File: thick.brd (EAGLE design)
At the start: 37 x 25 mm, 27 parts, among them J1 43045-0400, Q1 SI2319DDS-T1-GE3, U1 ATTINY85-20SU

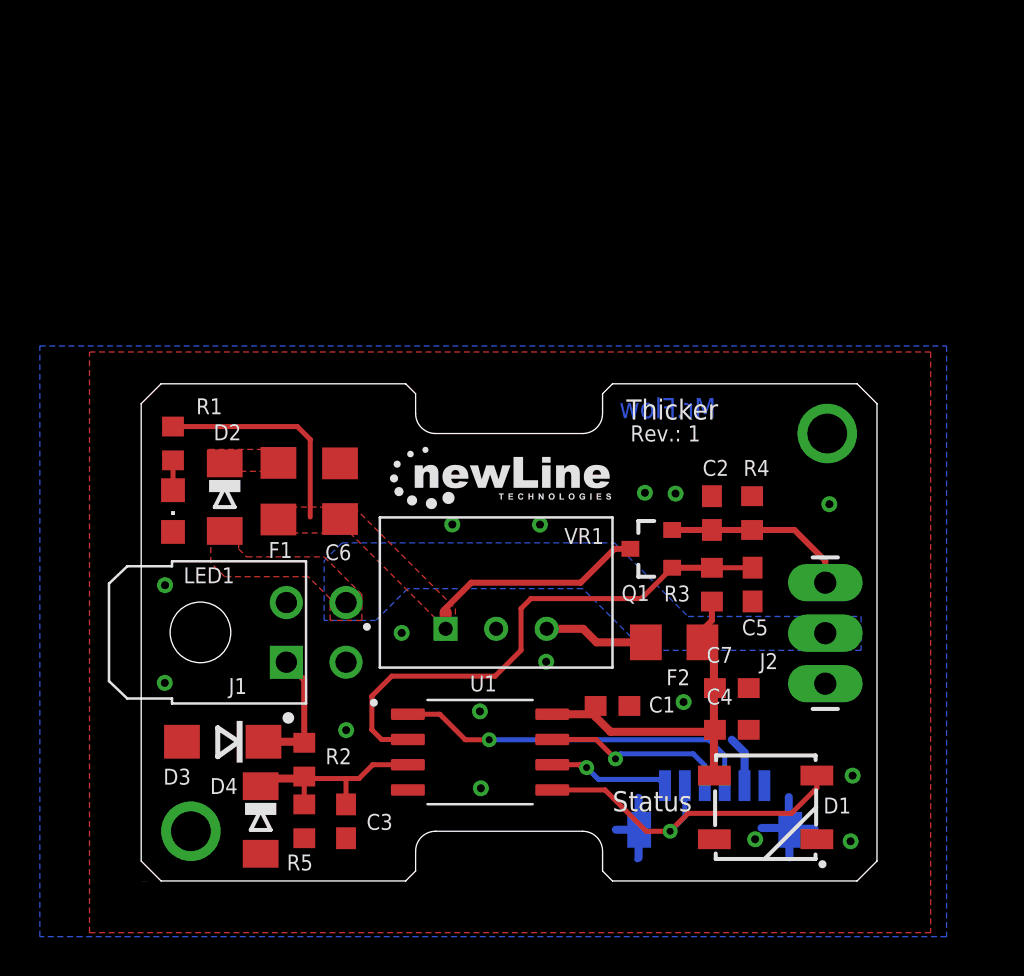
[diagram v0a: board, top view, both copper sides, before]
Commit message: Fixing
- sizes
- FPC connector
- Molex connector
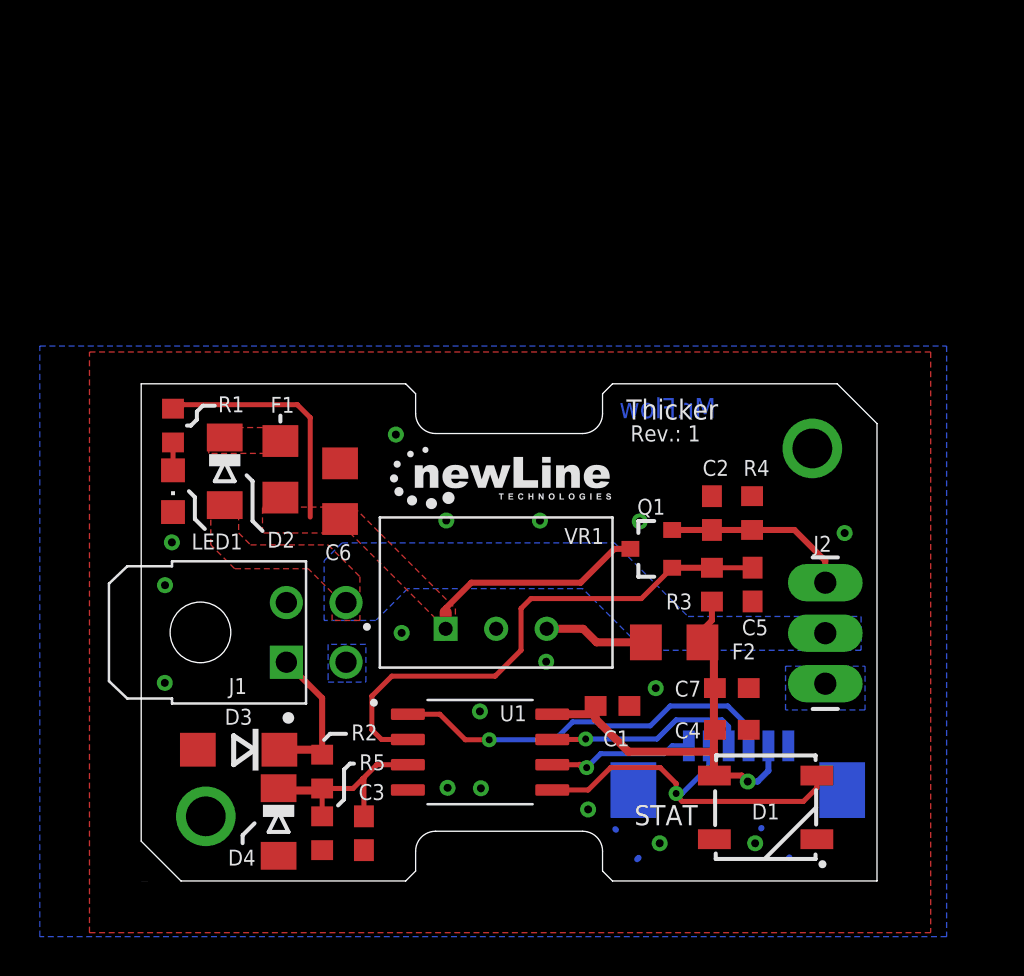
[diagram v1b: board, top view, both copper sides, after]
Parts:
- J4: value (none) -> F1003WR-S-06PT; device SparkFun-Connectors:1X06-1MM -> FloManEagle:1X06-1MM
- moved J4 2.33 mm to (30.0, 5.52)
- moved D2 1.30 mm to (4.20, 20.6)
- moved F1 1.10 mm to (7.00, 20.7)
- moved R5 1.08 mm to (9.10, 2.40)
- moved R2 1.08 mm to (9.10, 5.50)
- moved C3 1.08 mm to (11.2, 2.40)
- moved LED1 1.00 mm to (1.60, 19.6)
- moved D4 0.91 mm to (6.91, 2.96)
- moved R1 0.90 mm to (1.60, 22.9)
- moved D3 0.89 mm to (4.90, 6.60)
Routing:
- net GND: track 9.92 -> 0.22 mm, vias 18 -> 19
- net 5V: track 21.4 -> 23.6 mm, vias 0 -> 1
- net !RESET: track 18.3 -> 19.9 mm
- net MISO: track 6.11 -> 7.39 mm
- net VDD: track 22.8 -> 24.0 mm
- net SIGNAL: track 6.49 -> 7.65 mm
- net SCK: track 9.44 -> 10.4 mm
- net MOSI: track 18.3 -> 19.0 mm
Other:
- outline, holes or cut-outs redrawn
- board text added: "2021.06.30."
- board text added: "ISP"
- board text added: "STAT"
- board text removed: "2021.04.27."
- board text removed: "Programmer"
- board text removed: "Status"

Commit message: Javított végleges
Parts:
- added T1: (no value), transistor:SC59-BEC
- moved C5 5.16 mm to (25.6, 15.3)
- moved R3 5.06 mm to (25.6, 18.9)
- moved Q1 4.02 mm to (29.0, 19.0), turned to 270 degrees
- moved R4 3.73 mm to (34.4, 18.0)
- moved C2 3.54 mm to (32.2, 18.0)
- moved F2 0.36 mm to (27.1, 11.8)
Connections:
- removed net !IGN_EN: C5.1, Q1.1, R3.1, U1.2
- new net IGN_EN: C5.1, T1.B, U1.2
- new net N$1: Q1.1, R3.1, T1.C
- net 5V: no longer R3.2
- net GND: now also T1.E
- net IGNITION: now also Q1.3; no longer Q1.2
- net VDD: now also Q1.2, R3.2; no longer Q1.3
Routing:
- net !IGN_EN: track 26.8 -> 0.00 mm
- net IGN_EN: track 0.00 -> 23.1 mm
- net N$1: track 0.00 -> 8.14 mm
- net VDD: track 24.0 -> 28.2 mm
- net IGNITION: track 9.44 -> 7.77 mm
- net 5V: track 23.6 -> 22.0 mm
- net GND: vias 19 -> 18

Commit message: rev 2
new pcb design with gerbers
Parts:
- removed F2: (no value), adafruit:R1206
- removed VR1: VR05S05, TSR_1-24150:CONV_TSR_1-24150
- added C10, C8: 4.7uF, resistor:C1206
- added C11, C12: 0.1uF, resistor:C0603
- added C9: 100uF, resistor:E3,5-8
- added D5, D6: 0.5A/40V/420mV, SparkFun-DiscreteSemi:SOD-323
- added L1: TCK-047, TCK-047:TCK047
- added LED2: (no value), adafruit:CHIPLED_0805
- added R6: 10K, resistor:R0603
- added S1, S2: (no value), SparkFun-Switches:TACTILE_SWITCH_SMD_4.6X2.8MM
- added U$3: (no value), SparkFun-Aesthetics:ROHS_LOGO_0.18_IN
- added U$5: (no value), FloManEagle:MRFLOW_7_5MM
- added U2: TSR_0.5-2450, TSR_0.5-2450:TSR-0.5-2433
- C6: value 10uF -> 4.7uF
- C7: value 22uF -> 4.7uF; device resistor:C0603 -> resistor:C1206
- D3: value TVS -> tvs; device diode:DO214AC -> SparkFun-DiscreteSemi:SOD-323
- J1: value 43045-0400 -> (none); device 43045-0400:MOLEX_43045-0400 -> SparkFun-Connectors:1X03_LONGPADS
- moved J1 32.5 mm to (36.4, 18.5)
- moved U$1 32.3 mm to (25.0, 30.3)
- moved D3 31.4 mm to (32.2, 22.2), turned to 90 degrees
- moved J4 30.1 mm to (5.32, 22.8), flipped to the top, turned to 270 degrees
- moved D2 27.8 mm to (31.1, 13.4), turned to 0 degrees
- moved D4 27.3 mm to (29.6, 18.2)
- moved R2 26.5 mm to (29.6, 22.3)
- moved F1 26.1 mm to (31.2, 10.8), turned to 0 degrees
- moved U$2 25.1 mm to (20.0, 25.7)
- moved R5 24.6 mm to (27.5, 18.8)
- moved C6 23.5 mm to (27.1, 3.50), turned to 270 degrees
- moved C3 21.7 mm to (25.4, 18.8)
- moved U1 20.5 mm to (16.1, 26.9), turned to 180 degrees
- moved D1 19.9 mm to (20.0, 20.0)
- moved C4 19.1 mm to (15.3, 20.1), turned to 270 degrees
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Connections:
- new net N$2: C8.1, L1.2, U2.1
- new net N$5: D6.A, J4.2
- new net N$6: D3.C, D5.C, R2.1
- net !RESET: now also C11.1, S1.1, S1.2
- net 5V: now also C10.1, D6.C, R1.1, U2.3; no longer C7.1, F2.2, J4.2
- net AIN: now also U1.2; no longer U1.3
- net GND: now also C10.2, C11.2, C12.2, C8.2, C9.-, J1.2, LED2.C, S1.3, S1.4, S2.3, S2.4, U2.2; no longer J1.3, VR1.2
- net IGNITION: now also R6.1
- net IGN_EN: now also U1.3; no longer U1.2
- net MOSI: now also C12.1, S2.1, S2.2; no longer D1.4
- net N$4: now also LED2.A, R6.2; no longer F2.1, VR1.3
- net SCK: now also D1.4
- net SIGNAL: now also D5.A; no longer D3.C, R2.1
- net VCC: now also J1.3; no longer J1.4
- net VDD: now also C7.1, C9.+, L1.1; no longer R1.1, VR1.1
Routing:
- net IGN_EN: track 23.1 -> 5.33 mm
- net SCK: track 10.4 -> 23.7 mm, vias 1 -> 2
- net N$5: track 0.00 -> 9.62 mm
- net VDD: track 28.2 -> 19.7 mm, vias 0 -> 2
- net !RESET: track 19.9 -> 27.2 mm, vias 1 -> 2
- net IGNITION: track 7.77 -> 14.9 mm
- net AIN: track 10.4 -> 16.4 mm
- net N$6: track 0.00 -> 5.47 mm
- net 5V: track 22.0 -> 27.2 mm, vias 1 -> 0
- net MISO: track 7.39 -> 11.5 mm, vias 1 -> 0
- net N$1: track 8.14 -> 4.23 mm
- net N$4: track 5.65 -> 1.80 mm
- net MOSI: track 18.7 -> 22.5 mm, vias 1 -> 0
- net SIGNAL: track 7.65 -> 4.84 mm
- net N$3: track 1.40 -> 1.97 mm
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- added copper zone on layer 1, net N$2
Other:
- board size 37 x 25 mm -> 40 x 40 mm
- board text added: "2022.01.06."
- board text added: "FUNC"
- board text added: "INPUT"
- board text added: "Manufacturer: Szekely Florian ev. florian@mrflow.hu"
- board text added: "OUTPUT"
- board text added: "PROG"
- board text added: "PROTOTYPE"
- board text added: "PWR"
- board text added: "RESET"
- board text added: "Rev.: 2"
- board text added: "SGN"
- board text added: "VIN: 6.5-36VDC"
- board text removed: "2021.06.30."
- board text removed: "ISP"
- board text removed: "Mr.Flow"
- board text removed: "NewLine Kft. https://newline.hu/ Copyright (c) 2021"
- board text removed: "Rev.: 1"
- board text removed: "S/N:"
- board text removed: "VIN: 6.5-36VDC 2.5W"
